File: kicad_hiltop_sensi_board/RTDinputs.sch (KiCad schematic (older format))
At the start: 28 parts, among them SW2 SW_DIP_x04, SW3 SW_DIP_x04, SW4 SW_DIP_x04, SW5 SW_DIP_x04, U10 MAX31865, U11 MAX31865, U8 MAX31865, U9 MAX31865

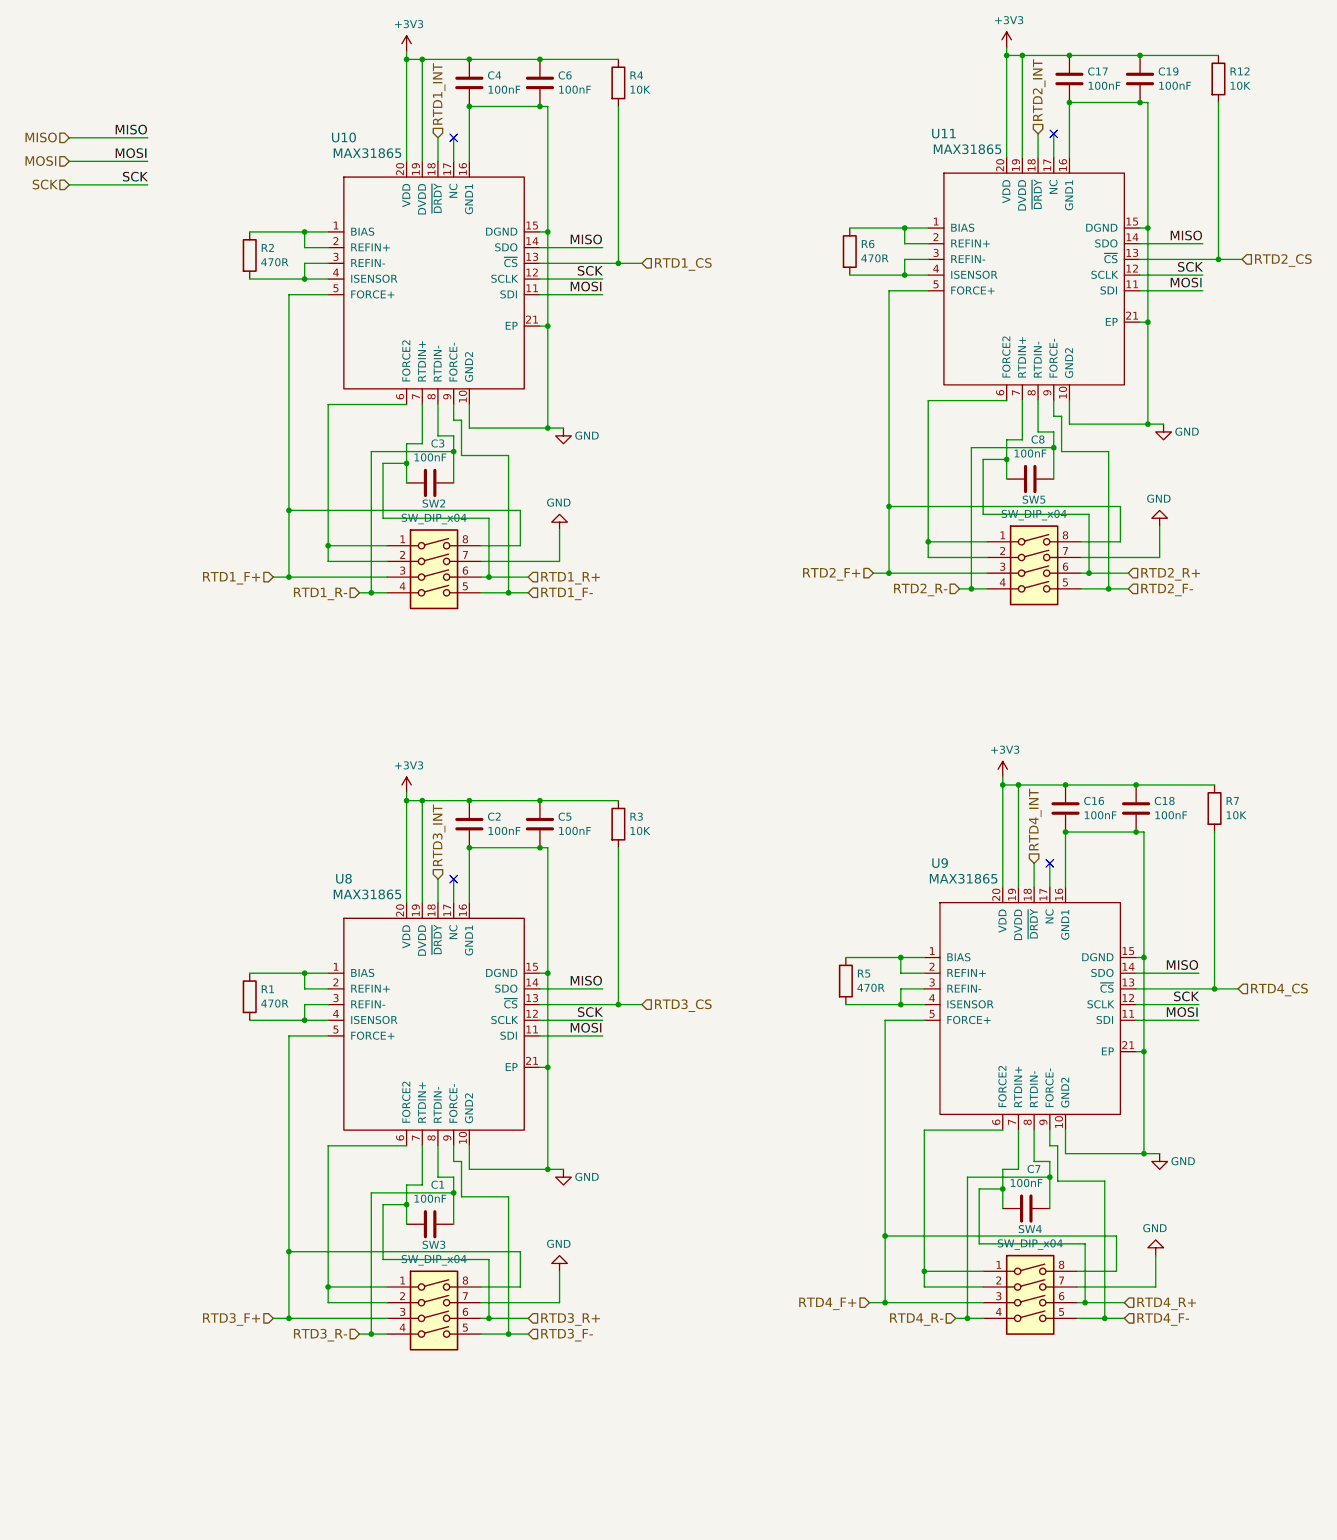
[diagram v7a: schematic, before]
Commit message: Sensi board schematic updated from comments
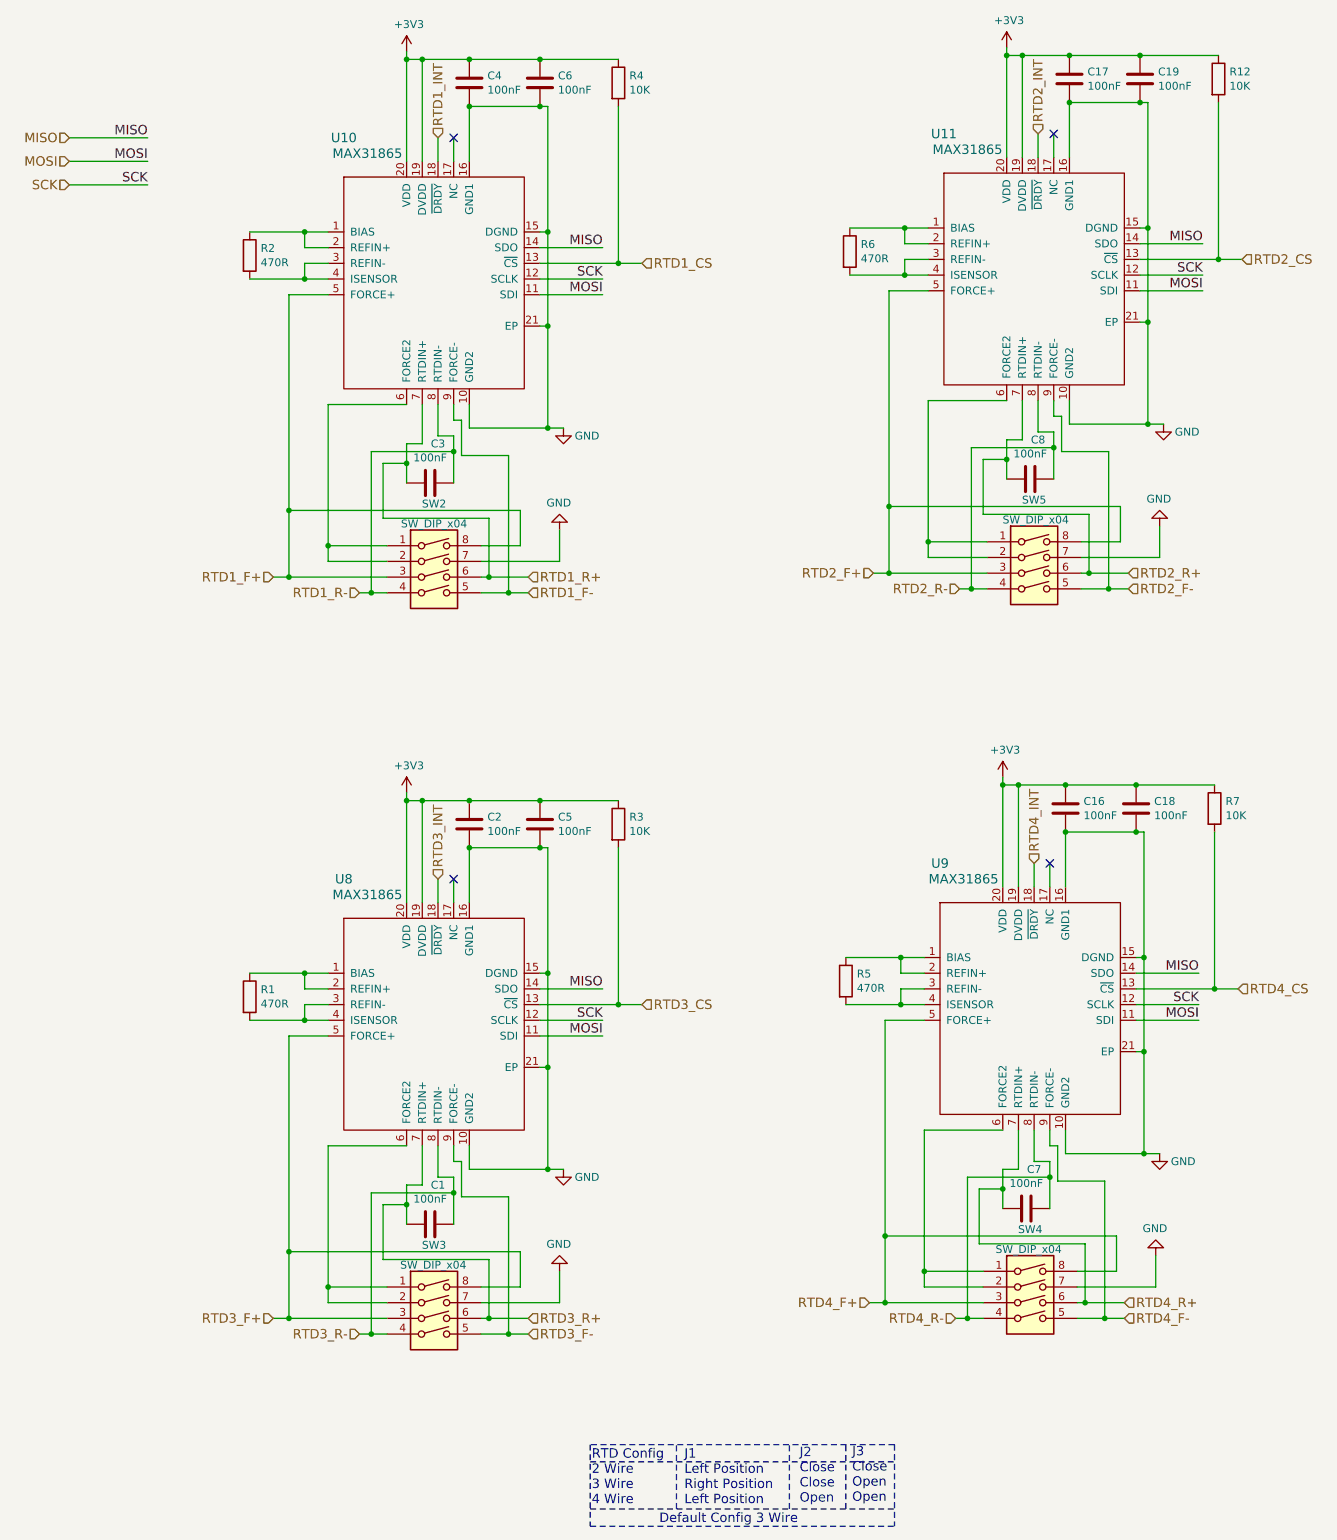
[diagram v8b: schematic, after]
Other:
- note added: "Default Config 3 Wire\n"
- note added: "J1\nLeft Position\nRight Position\nLeft Position"
- note added: "J2\nClose\nClose\nOpen"
- note added: "J3\nClose\nOpen\nOpen"
- note added: "RTD Config\n2 Wire\n3 Wire\n4 Wire"
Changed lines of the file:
@@
 $Descr A3 16535 11693
 encoding utf-8
-Sheet 10 11
+Sheet 9 11
 Title ""
 Date "2019-10-01"
@@
 P 3425 4650
 F 0 "SW2" H 3425 5117 50  0000 C CNN
-F 1 "SW_DIP_x04" H 3425 5026 50  0000 C CNN
+F 1 "SW_DIP_x04" H 3425 4990 50  0000 C CNN
 F 2 "Button_Switch_SMD:SW_DIP_SPSTx04_Slide_Copal_CHS-04B_W7.62mm_P1.27mm" H 3425 4650 50  0001 C CNN
 F 3 "" H 3425 4650 50  0001 C CNN
@@
 P 7250 4625
 F 0 "SW5" H 7250 5092 50  0000 C CNN
-F 1 "SW_DIP_x04" H 7250 5001 50  0000 C CNN
+F 1 "SW_DIP_x04" H 7260 4965 50  0000 C CNN
 F 2 "Button_Switch_SMD:SW_DIP_SPSTx04_Slide_Copal_CHS-04B_W7.62mm_P1.27mm" H 7250 4625 50  0001 C CNN
 F 3 "" H 7250 4625 50  0001 C CNN
@@
 P 3425 9375
 F 0 "SW3" H 3425 9842 50  0000 C CNN
-F 1 "SW_DIP_x04" H 3425 9751 50  0000 C CNN
+F 1 "SW_DIP_x04" H 3420 9715 50  0000 C CNN
 F 2 "Button_Switch_SMD:SW_DIP_SPSTx04_Slide_Copal_CHS-04B_W7.62mm_P1.27mm" H 3425 9375 50  0001 C CNN
 F 3 "" H 3425 9375 50  0001 C CNN
@@
 P 7225 9275
 F 0 "SW4" H 7225 9742 50  0000 C CNN
-F 1 "SW_DIP_x04" H 7225 9651 50  0000 C CNN
+F 1 "SW_DIP_x04" H 7215 9615 50  0000 C CNN
 F 2 "Button_Switch_SMD:SW_DIP_SPSTx04_Slide_Copal_CHS-04B_W7.62mm_P1.27mm" H 7225 9275 50  0001 C CNN
 F 3 "" H 7225 9275 50  0001 C CNN
@@
 	7700 9375 7825 9375
 Connection ~ 7700 9375
+Text Notes 4430 10570 0    60   ~ 0
+RTD Config\n2 Wire\n3 Wire\n4 Wire
+Text Notes 5020 10570 0    60   ~ 0
+J1\nLeft Position\nRight Position\nLeft Position
+Text Notes 5755 10560 0    60   ~ 0
+J2\nClose\nClose\nOpen
+Text Notes 6090 10555 0    60   ~ 0
+J3\nClose\nOpen\nOpen
+Wire Notes Line
+	4420 10590 6360 10590
+Wire Notes Line
+	6360 10180 4420 10180
+Wire Notes Line
+	4420 10290 6360 10290
+Wire Notes Line
+	6050 10590 6050 10180
+Wire Notes Line
+	5690 10590 5690 10180
+Wire Notes Line
+	4970 10590 4970 10180
+Text Notes 4860 10690 0    60   ~ 0
+Default Config 3 Wire\n
+Wire Notes Line
+	4420 10700 6360 10700
+Wire Notes Line
+	6360 10180 6360 10700
+Wire Notes Line
+	4420 10180 4420 10700
 $EndSCHEMATC
